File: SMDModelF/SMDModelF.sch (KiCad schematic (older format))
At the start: 45 parts, among them J1 Model F Ribbon Cable, J2 PadsToShort, J3 EXPANSION HEADER, J4 3178 Ribbon Cable, J6 MODEL F AT LOCKLIGHTS HEADER, U1 MCP4921-E, U2 LM339A, U3 74AHC595, U4 74AHC595, U5 ProMicro, U6 LM339A

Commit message: Added vertical footprint, but with horizontal 3d part for solenoid driver header.
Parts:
- J3: footprint Connector_PinHeader_2.54mm:PinHeader_2x03_P2.54mm_Vertical -> TH-XWhatsIt:PinHeader_2x03_P2.54mm_Vertical_3dhorizontal
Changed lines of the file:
@@
 F 0 "J3" H 8125 5867 50  0000 C CNN
 F 1 "EXPANSION HEADER" H 8125 5776 50  0000 C CNN
-F 2 "Connector_PinHeader_2.54mm:PinHeader_2x03_P2.54mm_Vertical" H 8075 5550 50  0001 C CNN
+F 2 "TH-XWhatsIt:PinHeader_2x03_P2.54mm_Vertical_3dhorizontal" H 8075 5550 50  0001 C CNN
 F 3 "~" H 8075 5550 50  0001 C CNN
 	1    8075 5550

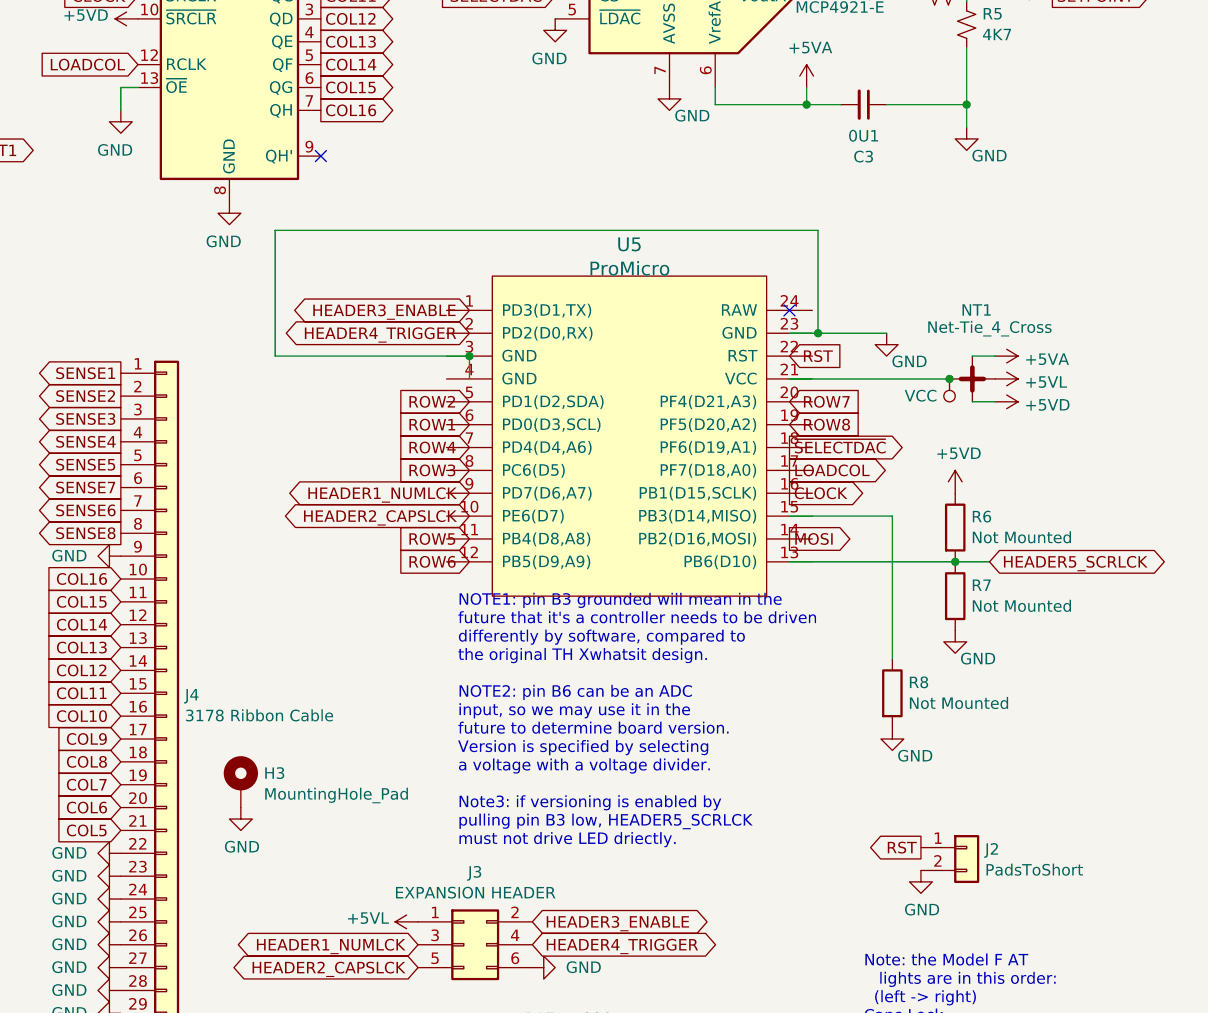
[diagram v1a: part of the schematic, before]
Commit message: Updated pro micro schematic symbol, and added PDF schematics
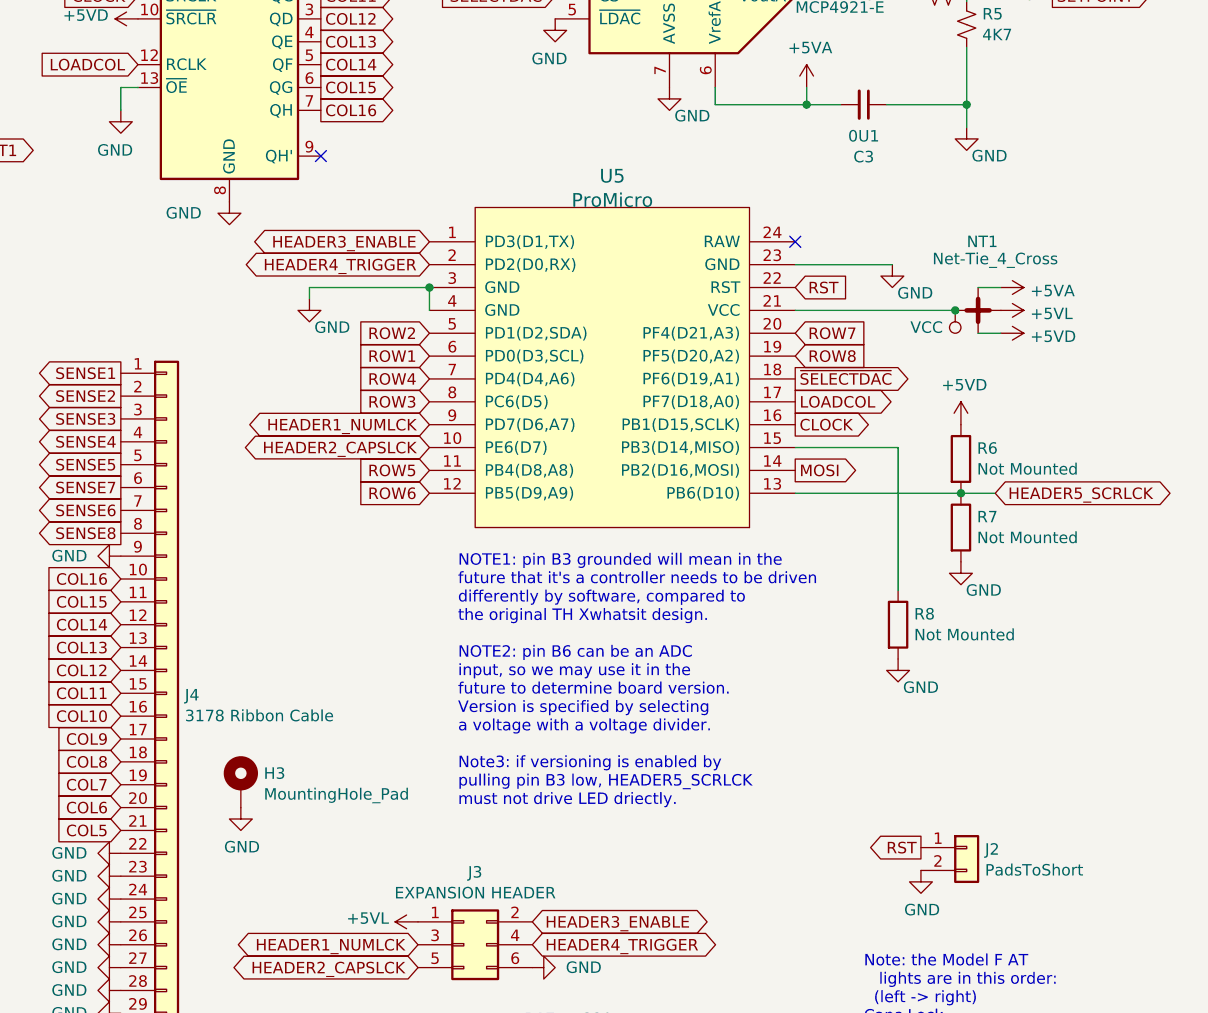
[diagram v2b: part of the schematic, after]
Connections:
- wire segments 93 -> 90
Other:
- moved on the sheet: NT1, R6, R7, R8, U5

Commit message: Updated 100k resistor and shift register LCSC part numbers
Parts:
- R10, R11, R12, R13, R14, R15, R16, R9: LCSC C17407 -> C149504
- U3, U4: LCSC C5520 -> C2682116
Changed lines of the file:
@@
 F 2 "Package_SO:SOIC-16_3.9x9.9mm_P1.27mm" H 5275 1575 50  0001 C CNN
 F 3 "https://assets.nexperia.com/documents/data-sheet/74HC_HCT595.pdf" H 5275 1575 50  0001 C CNN
-F 4 "C5520" H 5275 1575 50  0001 C CNN "LCSC"
+F 4 "C2682116" H 5275 1575 50  0001 C CNN "LCSC"
 	1    5275 1575
 	1    0    0    -1
@@
 F 2 "Package_SO:SOIC-16_3.9x9.9mm_P1.27mm" H 7050 1600 50  0001 C CNN
 F 3 "https://assets.nexperia.com/documents/data-sheet/74HC_HCT595.pdf" H 7050 1600 50  0001 C CNN
-F 4 "C5520" H 7050 1600 50  0001 C CNN "LCSC"
+F 4 "C2682116" H 7050 1600 50  0001 C CNN "LCSC"
 	1    7050 1600
 	1    0    0    -1
@@
 F 2 "Resistor_SMD:R_0805_2012Metric_Pad1.15x1.40mm_HandSolder" V 1380 1325 50  0001 C CNN
 F 3 "~" H 1450 1325 50  0001 C CNN
-F 4 "C17407" H 1450 1325 50  0001 C CNN "LCSC"
+F 4 "C149504" H 1450 1325 50  0001 C CNN "LCSC"
 	1    1450 1325
 	1    0    0    -1
@@
 F 2 "Resistor_SMD:R_0805_2012Metric_Pad1.15x1.40mm_HandSolder" V 1380 1925 50  0001 C CNN
 F 3 "~" H 1450 1925 50  0001 C CNN
-F 4 "C17407" H 1450 1925 50  0001 C CNN "LCSC"
+F 4 "C149504" H 1450 1925 50  0001 C CNN "LCSC"
 	1    1450 1925
 	1    0    0    -1
@@
 F 2 "Resistor_SMD:R_0805_2012Metric_Pad1.15x1.40mm_HandSolder" V 1380 2525 50  0001 C CNN
 F 3 "~" H 1450 2525 50  0001 C CNN
-F 4 "C17407" H 1450 2525 50  0001 C CNN "LCSC"
+F 4 "C149504" H 1450 2525 50  0001 C CNN "LCSC"
 	1    1450 2525
 	1    0    0    -1
@@
 F 2 "Resistor_SMD:R_0805_2012Metric_Pad1.15x1.40mm_HandSolder" V 1380 3125 50  0001 C CNN
 F 3 "~" H 1450 3125 50  0001 C CNN
-F 4 "C17407" H 1450 3125 50  0001 C CNN "LCSC"
+F 4 "C149504" H 1450 3125 50  0001 C CNN "LCSC"
 	1    1450 3125
 	1    0    0    -1
@@
 F 2 "Resistor_SMD:R_0805_2012Metric_Pad1.15x1.40mm_HandSolder" V 1380 4050 50  0001 C CNN
 F 3 "~" H 1450 4050 50  0001 C CNN
-F 4 "C17407" H 1450 4050 50  0001 C CNN "LCSC"
+F 4 "C149504" H 1450 4050 50  0001 C CNN "LCSC"
 	1    1450 4050
 	1    0    0    -1
@@
 F 2 "Resistor_SMD:R_0805_2012Metric_Pad1.15x1.40mm_HandSolder" V 1380 4650 50  0001 C CNN
 F 3 "~" H 1450 4650 50  0001 C CNN
-F 4 "C17407" H 1450 4650 50  0001 C CNN "LCSC"
+F 4 "C149504" H 1450 4650 50  0001 C CNN "LCSC"
 	1    1450 4650
 	1    0    0    -1
@@
 F 2 "Resistor_SMD:R_0805_2012Metric_Pad1.15x1.40mm_HandSolder" V 1380 5250 50  0001 C CNN
 F 3 "~" H 1450 5250 50  0001 C CNN
-F 4 "C17407" H 1450 5250 50  0001 C CNN "LCSC"
+F 4 "C149504" H 1450 5250 50  0001 C CNN "LCSC"
 	1    1450 5250
 	1    0    0    -1
@@
 F 2 "Resistor_SMD:R_0805_2012Metric_Pad1.15x1.40mm_HandSolder" V 1380 5850 50  0001 C CNN
 F 3 "~" H 1450 5850 50  0001 C CNN
-F 4 "C17407" H 1450 5850 50  0001 C CNN "LCSC"
+F 4 "C149504" H 1450 5850 50  0001 C CNN "LCSC"
 	1    1450 5850
 	1    0    0    -1

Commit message: Revert part of commit 'Updated 100k resistor and shift register LCSC part numbers' (the shift register BOM changes only)
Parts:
- U3, U4: LCSC C2682116 -> C5520
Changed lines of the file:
@@
 F 2 "Package_SO:SOIC-16_3.9x9.9mm_P1.27mm" H 5275 1575 50  0001 C CNN
 F 3 "https://assets.nexperia.com/documents/data-sheet/74HC_HCT595.pdf" H 5275 1575 50  0001 C CNN
-F 4 "C2682116" H 5275 1575 50  0001 C CNN "LCSC"
+F 4 "C5520" H 5275 1575 50  0001 C CNN "LCSC"
 	1    5275 1575
 	1    0    0    -1
@@
 F 2 "Package_SO:SOIC-16_3.9x9.9mm_P1.27mm" H 7050 1600 50  0001 C CNN
 F 3 "https://assets.nexperia.com/documents/data-sheet/74HC_HCT595.pdf" H 7050 1600 50  0001 C CNN
-F 4 "C2682116" H 7050 1600 50  0001 C CNN "LCSC"
+F 4 "C5520" H 7050 1600 50  0001 C CNN "LCSC"
 	1    7050 1600
 	1    0    0    -1
